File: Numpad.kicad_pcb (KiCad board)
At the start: 2 copper layers, 76.2 x 97.6 mm, 56 parts, among them J1 USB_B_Mini, SW0 0, SW1 1, SW2 2, SW3 3, SW4 4, SW5 5, SW6 6, SW7 7, SW8 8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

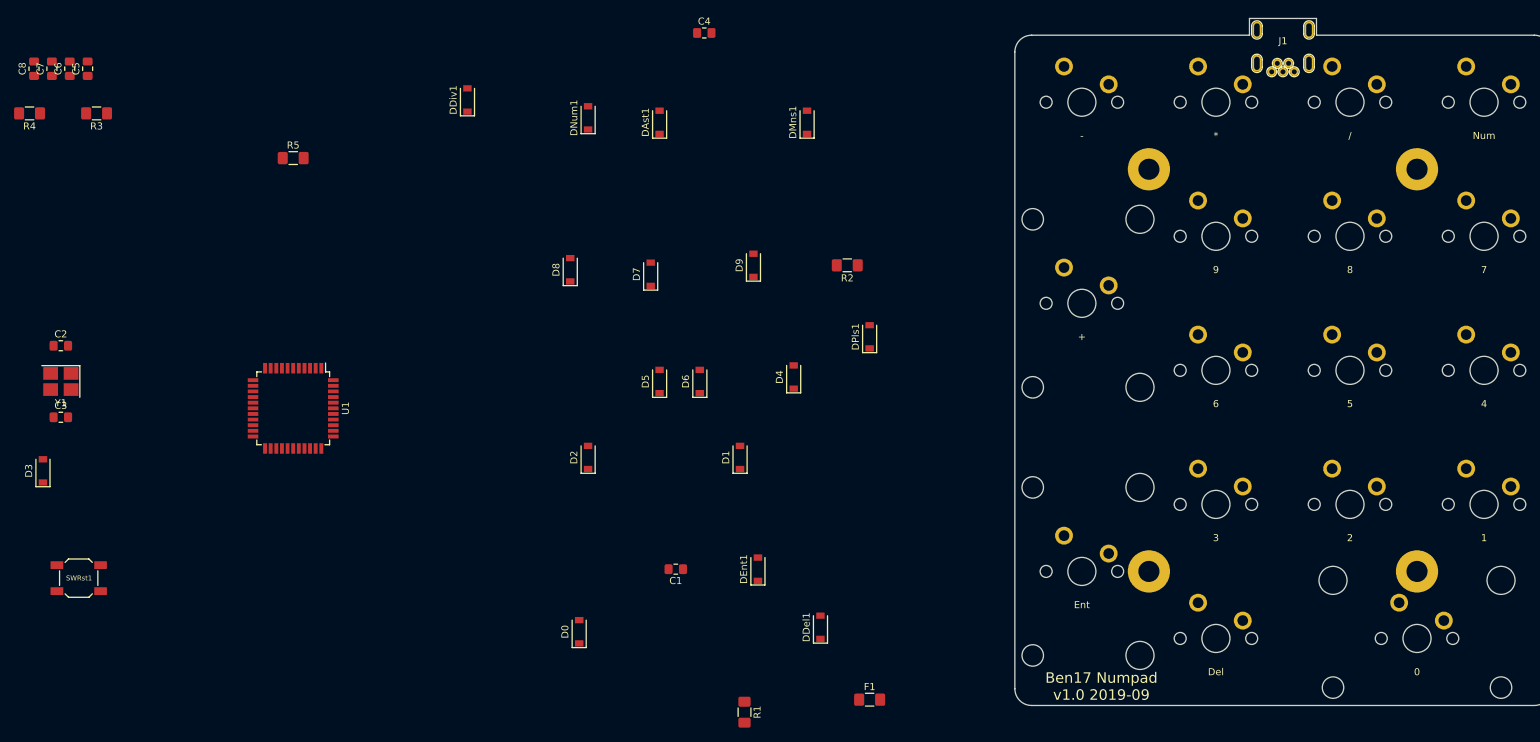
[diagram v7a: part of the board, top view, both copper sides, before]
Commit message: moved some components around
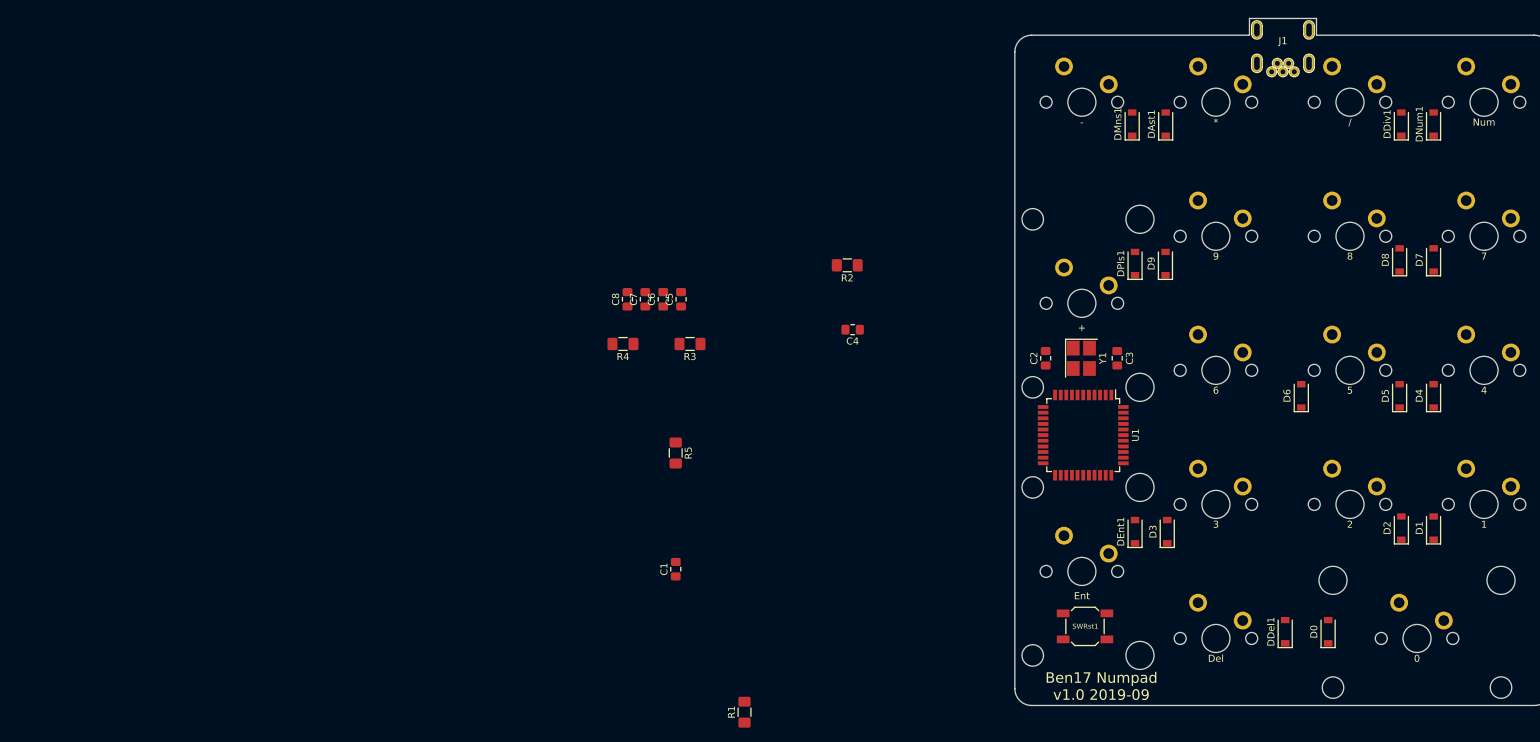
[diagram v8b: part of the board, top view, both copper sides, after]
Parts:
- removed F1: 500mA, Fuse:Fuse_1206_3216Metric_Pad1.42x1.75mm_HandSolder
- removed H1, H2, H3, H4: MountingHole, MountingHole:MountingHole_3mm_Pad
- moved D3 160.0 mm to (175.0, 111.5)
- moved C3 150.3 mm to (167.9, 86.9), turned to 90 degrees
- moved Y1 145.1 mm to (162.8, 86.9), turned to 270 degrees
- moved SWRst1 143.2 mm to (163.3, 125.0)
- moved C2 140.0 mm to (157.7, 86.9), turned to 90 degrees
- moved DDiv1 132.8 mm to (208.3, 53.6)
- moved DNum1 120.1 mm to (212.9, 53.6)
- moved D8 117.9 mm to (208.0, 72.9)
- moved D2 116.0 mm to (208.3, 111.0)
- moved U1 112.3 mm to (163.1, 97.8)
- moved D7 111.3 mm to (212.9, 72.9)
- moved D0 106.4 mm to (197.9, 125.7)
- moved D5 105.2 mm to (208.0, 92.2)
- moved D1 99.1 mm to (212.9, 111.0)
- moved D4 91.0 mm to (212.9, 92.2)
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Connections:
- J1 pad 1: VCC -> +5V
